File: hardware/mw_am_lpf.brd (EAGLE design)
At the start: 38.1 x 33 mm, 15 parts, among them J1 VGA_DB25

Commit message: added PTH for VGA connector tabs; LPF has SMA jack
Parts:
- J1: value VGA_DB25 -> VGA_DB15
- U$19: value EDGE_LAUNCH_JACK -> SMA
- moved U$19 3.18 mm to (38.1, 16.5), turned to 0 degrees
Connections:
- net GND: now also J1.TAB@1, J1.TAB@2, U$19.GND@10, U$19.GND@11, U$19.GND@12, U$19.GND@3, U$19.GND@4, U$19.GND@5, U$19.GND@6, U$19.GND@7, U$19.GND@8, U$19.GND@9, U$19.SHIELD@1, U$19.SHIELD@2
- net N$5: now also U$19.CENTER; no longer U$19.SIG
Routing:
- net GND: track 8.35 -> 0.00 mm, vias 35 -> 31
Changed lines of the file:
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@@
 </class>
 </classes>
-<designrules name="oshpark-2layer">
+<designrules name="oshpark-2layer *">
 <description language="en">&lt;b&gt;OSH Park Design Rules&lt;/b&gt;
 &lt;p&gt;
@@
 <param name="mtCopper" value="0.035559375mm 0.0356mm 0.0356mm 0.0356mm 0.0356mm 0.0356mm 0.0356mm 0.0356mm 0.0356mm 0.0356mm 0.0356mm 0.0356mm 0.0356mm 0.0356mm 0.0356mm 0.035559375mm"/>
 <param name="mtIsolate" value="1.6mm 0.1499mm 0.2007mm 0.1499mm 0.2007mm 0.1499mm 0.2007mm 0.1499mm 0.2007mm 0.1499mm 0.2007mm 0.1499mm 0.2007mm 0.1499mm 0.2007mm"/>
-<param name="mdWireWire" value="6mil"/>
-<param name="mdWirePad" value="6mil"/>
-<param name="mdWireVia" value="6mil"/>
-<param name="mdPadPad" value="6mil"/>
-<param name="mdPadVia" value="6mil"/>
-<param name="mdViaVia" value="6mil"/>
+<param name="mdWireWire" value="8mil"/>
+<param name="mdWirePad" value="8mil"/>
+<param name="mdWireVia" value="8mil"/>
+<param name="mdPadPad" value="8mil"/>
+<param name="mdPadVia" value="8mil"/>
+<param name="mdViaVia" value="8mil"/>
 <param name="mdSmdPad" value="6mil"/>
 <param name="mdSmdVia" value="6mil"/>
@@
 <element name="U$8" library="mw-voice-marker" package="R0805" value="27" x="19.05" y="27.305"/>
 <element name="U$9" library="mw-voice-marker" package="R0805" value="420" x="19.05" y="24.765" rot="R180"/>
-<element name="J1" library="mw-voice-marker" package="VGA_PCB_MALE" value="VGA_DB25" x="11.43" y="16.51" rot="R270"/>
-<element name="U$19" library="mw-voice-marker" package="EDGE_LAUNCH_RF_CON" value="EDGE_LAUNCH_JACK" x="34.925" y="16.51" rot="R90"/>
+<element name="J1" library="mw-voice-marker" package="VGA_PCB_MALE" value="VGA_DB15" x="11.43" y="16.51" rot="R270"/>
+<element name="U$19" library="mw-voice-marker" package="EDGE_LAUNCH_RF_CON" value="SMA" x="38.1" y="16.51"/>
 </elements>
 <signals>
@@
 <contactref element="U$4" pad="P$1"/>
 <contactref element="U$6" pad="P$2"/>
-<polygon width="0.1524" layer="1">
+<polygon width="0.4064" layer="1">
 <vertex x="0" y="0"/>
 <vertex x="38.1" y="0"/>
@@
 <contactref element="J1" pad="5"/>
 <contactref element="J1" pad="10"/>
-<contactref element="U$19" pad="GND@1"/>
-<contactref element="U$19" pad="GND@2"/>
 <via x="1.27" y="1.27" extent="1-16" drill="0.5"/>
 <via x="5.08" y="1.27" extent="1-16" drill="0.5"/>
@@
 <via x="31.75" y="31.75" extent="1-16" drill="0.5"/>
 <via x="35.56" y="31.75" extent="1-16" drill="0.5"/>
-<wire x1="34.925" y1="21.59" x2="30.48" y2="20.955" width="1.016" layer="1"/>
-<wire x1="34.925" y1="11.43" x2="31.115" y2="10.795" width="1.016" layer="1"/>
 <via x="36.83" y="28.575" extent="1-16" drill="0.5"/>
 <via x="36.83" y="25.4" extent="1-16" drill="0.5"/>
 <via x="36.83" y="2.54" extent="1-16" drill="0.5"/>
 <via x="36.83" y="5.715" extent="1-16" drill="0.5"/>
-<via x="36.195" y="8.89" extent="1-16" drill="0.5"/>
-<via x="36.195" y="24.13" extent="1-16" drill="0.5"/>
-<via x="33.655" y="24.13" extent="1-16" drill="0.5"/>
-<via x="33.655" y="8.89" extent="1-16" drill="0.5"/>
+<contactref element="U$19" pad="GND@8"/>
+<contactref element="U$19" pad="GND@1"/>
+<contactref element="U$19" pad="GND@3"/>
+<contactref element="U$19" pad="GND@7"/>
+<contactref element="U$19" pad="GND@9"/>
+<contactref element="U$19" pad="GND@12"/>
+<contactref element="U$19" pad="SHIELD@1"/>
+<contactref element="U$19" pad="GND@4"/>
+<contactref element="U$19" pad="GND@11"/>
+<contactref element="U$19" pad="GND@6"/>
+<contactref element="U$19" pad="SHIELD@2"/>
+<contactref element="U$19" pad="GND@10"/>
+<contactref element="U$19" pad="GND@2"/>
+<contactref element="U$19" pad="GND@5"/>
+<contactref element="J1" pad="TAB@1"/>
+<contactref element="J1" pad="TAB@2"/>
 </signal>
 <signal name="N$1">
@@
 <contactref element="U$5" pad="P$1"/>
 <contactref element="U$6" pad="P$1"/>
-<contactref element="U$19" pad="SIG"/>
 <wire x1="29.45" y1="19.05" x2="29.45" y2="16.51" width="1.016" layer="1"/>
-<wire x1="34.925" y1="16.51" x2="29.45" y2="16.51" width="1.016" layer="1"/>
+<contactref element="U$19" pad="CENTER"/>
+<wire x1="35.225" y1="16.51" x2="29.45" y2="16.51" width="1.0414" layer="1"/>
 </signal>
 <signal name="N$6">

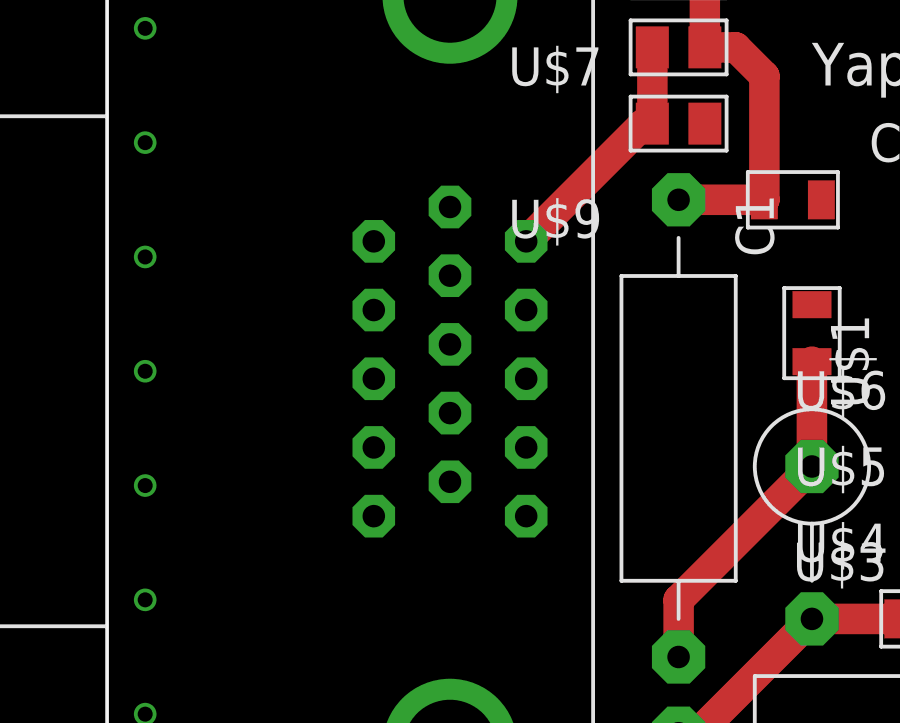
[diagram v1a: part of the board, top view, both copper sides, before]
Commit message: updated VGA connector footprint
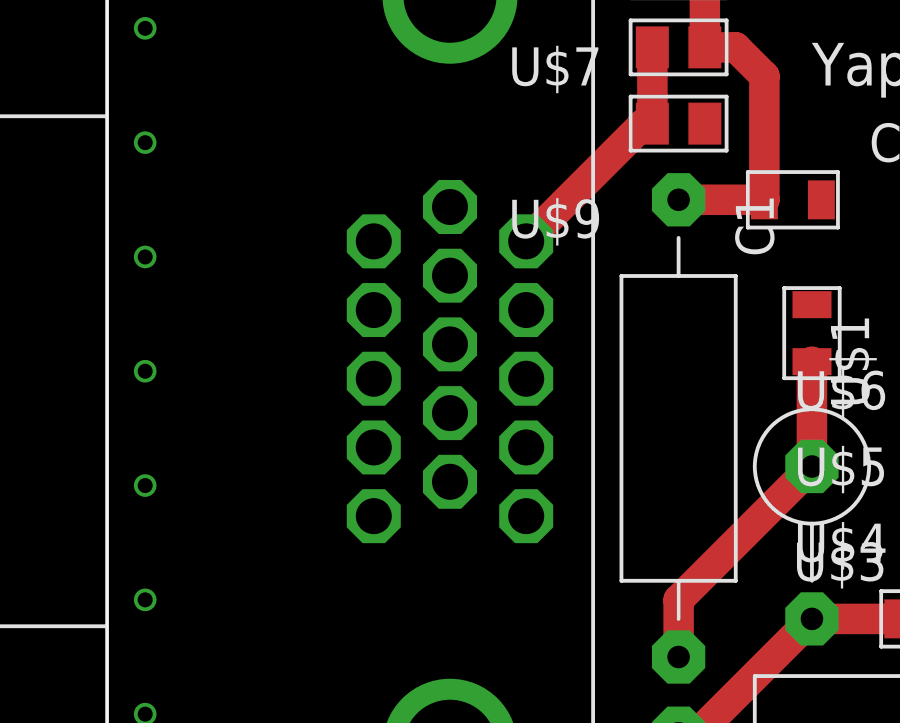
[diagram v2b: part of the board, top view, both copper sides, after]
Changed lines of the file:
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@@
 <contactref element="U$4" pad="P$1"/>
 <contactref element="U$6" pad="P$2"/>
-<polygon width="0.4064" layer="1">
+<polygon width="0.1524" layer="1">
 <vertex x="0" y="0"/>
 <vertex x="38.1" y="0"/>
